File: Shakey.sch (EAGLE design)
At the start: 82 parts, among them CN1 CONN_USB-4UCON-11071, CN2 ISP, U1 ATMEGA32U4-AU, U2 ICM-20689, U3 AP2210K-3.3TRG1, Y1 16Mhz

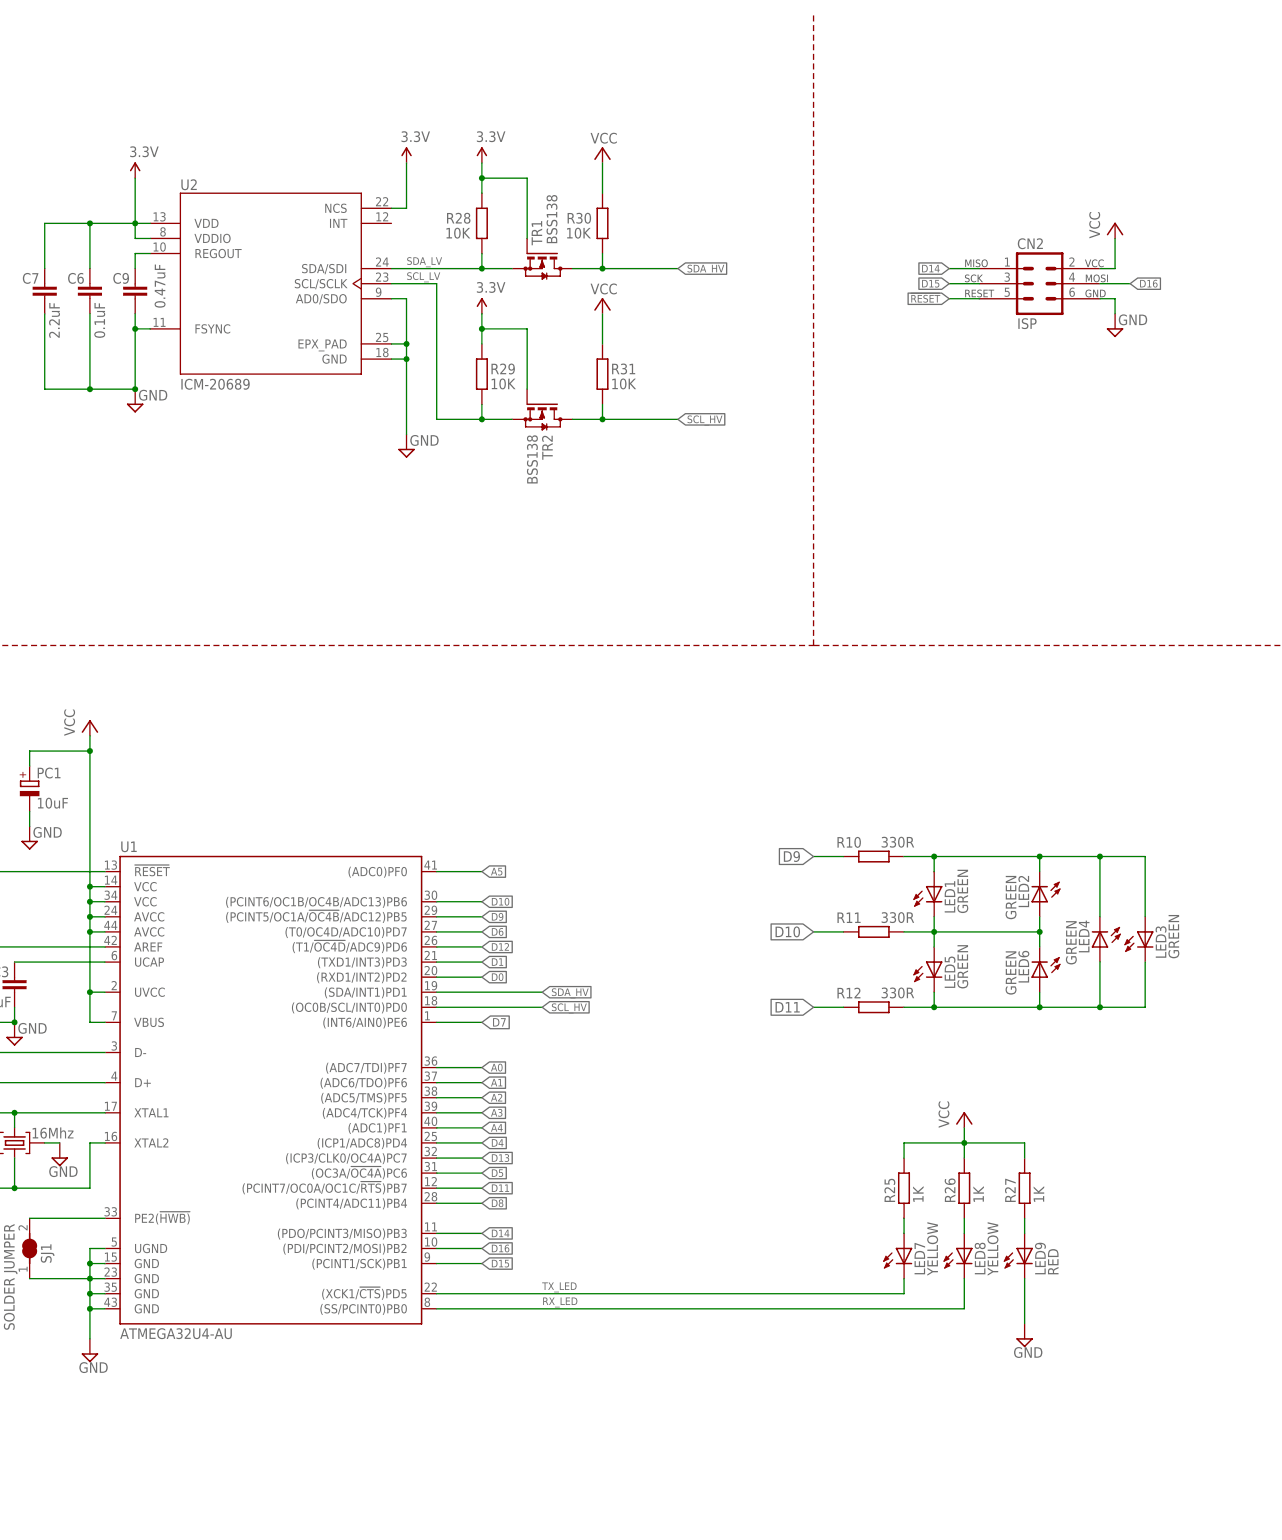
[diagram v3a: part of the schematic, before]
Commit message: added LM75
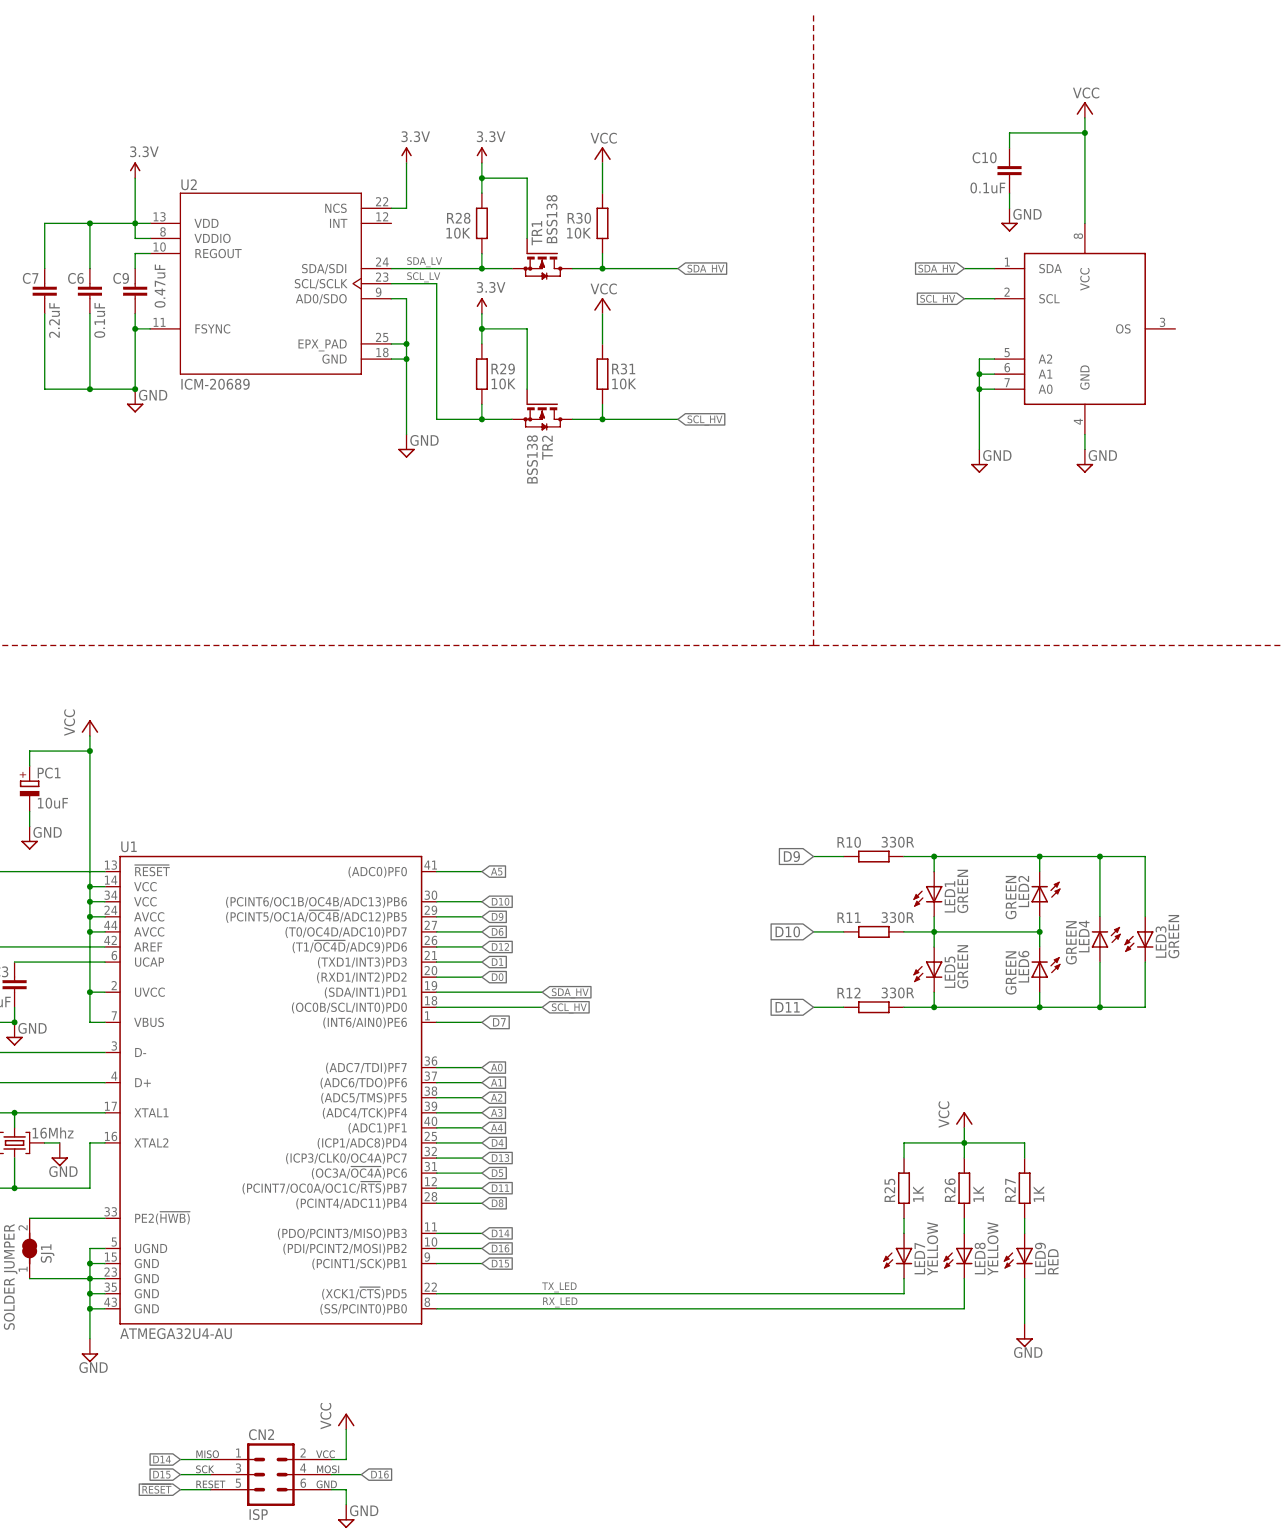
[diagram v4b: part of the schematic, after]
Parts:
- added C10: 0.1uF, rcl:C-EUC0603
- added U$6: LM75AD, SixthLogic:LM75AD
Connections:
- net GND: now also C10.1, U$6.A0, U$6.A1, U$6.A2, U$6.GND
- net SCL_HV: now also U$6.SCL
- net SDA_HV: now also U$6.SDA
- net VCC: now also C10.2, U$6.VCC
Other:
- moved on the sheet: CN2
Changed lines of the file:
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@@
 <part name="U$5" library="SixthLogic" deviceset="3.3V" device=""/>
 <part name="P+10" library="supply1" deviceset="VCC" device=""/>
+<part name="U$6" library="SixthLogic" deviceset="LM75" device="AD"/>
+<part name="SUPPLY16" library="supply2" deviceset="GND" device=""/>
+<part name="P+12" library="supply1" deviceset="VCC" device=""/>
+<part name="SUPPLY17" library="supply2" deviceset="GND" device=""/>
+<part name="C10" library="rcl" deviceset="C-EU" device="C0603" value="0.1uF"/>
+<part name="SUPPLY18" library="supply2" deviceset="GND" device=""/>
 </parts>
 <sheets>
@@
 </instance>
 <instance part="P+4" gate="VCC" x="386.08" y="149.86"/>
-<instance part="CN2" gate="G$1" x="279.4" y="228.6"/>
-<instance part="P+5" gate="VCC" x="292.1" y="238.76"/>
-<instance part="SUPPLY8" gate="GND" x="292.1" y="220.98" smashed="yes">
-<attribute name="VALUE" x="292.608" y="221.615" size="1.778" layer="96"/>
+<instance part="CN2" gate="G$1" x="149.86" y="27.94"/>
+<instance part="P+5" gate="VCC" x="162.56" y="38.1"/>
+<instance part="SUPPLY8" gate="GND" x="162.56" y="20.32" smashed="yes">
+<attribute name="VALUE" x="163.068" y="20.955" size="1.778" layer="96"/>
 </instance>
 <instance part="G" gate="G$1" x="365.76" y="167.64" smashed="yes">
@@
 <instance part="P+10" gate="VCC" x="205.74" y="226.06" smashed="yes">
 <attribute name="VALUE" x="208.28" y="228.6" size="1.778" layer="96" rot="R180"/>
+</instance>
+<instance part="U$6" gate="G$1" x="287.02" y="220.98"/>
+<instance part="SUPPLY16" gate="GND" x="287.02" y="198.12" smashed="yes">
+<attribute name="VALUE" x="287.528" y="198.755" size="1.778" layer="96"/>
+</instance>
+<instance part="P+12" gate="VCC" x="287.02" y="259.08" smashed="yes">
+<attribute name="VALUE" x="289.56" y="261.62" size="1.778" layer="96" rot="R180"/>
+</instance>
+<instance part="SUPPLY17" gate="GND" x="269.24" y="198.12" smashed="yes">
+<attribute name="VALUE" x="269.748" y="198.755" size="1.778" layer="96"/>
+</instance>
+<instance part="C10" gate="G$1" x="274.32" y="246.38" smashed="yes" rot="R180">
+<attribute name="NAME" x="267.97" y="248.92" size="1.778" layer="95"/>
+<attribute name="VALUE" x="267.589" y="243.84" size="1.778" layer="96"/>
+</instance>
+<instance part="SUPPLY18" gate="GND" x="274.32" y="238.76" smashed="yes">
+<attribute name="VALUE" x="274.828" y="239.395" size="1.778" layer="96"/>
 </instance>
 </instances>
@@
 <segment>
 <pinref part="CN2" gate="G$1" pin="6"/>
-<wire x1="289.56" y1="226.06" x2="292.1" y2="226.06" width="0.1524" layer="91"/>
-<wire x1="292.1" y1="226.06" x2="292.1" y2="223.52" width="0.1524" layer="91"/>
+<wire x1="160.02" y1="25.4" x2="162.56" y2="25.4" width="0.1524" layer="91"/>
+<wire x1="162.56" y1="25.4" x2="162.56" y2="22.86" width="0.1524" layer="91"/>
 <pinref part="SUPPLY8" gate="GND" pin="GND"/>
 </segment>
@@
 <pinref part="SUPPLY15" gate="GND" pin="GND"/>
 <wire x1="109.22" y1="139.7" x2="109.22" y2="137.16" width="0.1524" layer="91"/>
+</segment>
+<segment>
+<pinref part="U$6" gate="G$1" pin="GND"/>
+<pinref part="SUPPLY16" gate="GND" pin="GND"/>
+<wire x1="287.02" y1="203.2" x2="287.02" y2="200.66" width="0.1524" layer="91"/>
+</segment>
+<segment>
+<pinref part="U$6" gate="G$1" pin="A2"/>
+<wire x1="271.78" y1="215.9" x2="269.24" y2="215.9" width="0.1524" layer="91"/>
+<wire x1="269.24" y1="215.9" x2="269.24" y2="213.36" width="0.1524" layer="91"/>
+<pinref part="U$6" gate="G$1" pin="A1"/>
+<wire x1="269.24" y1="213.36" x2="269.24" y2="210.82" width="0.1524" layer="91"/>
+<wire x1="269.24" y1="210.82" x2="269.24" y2="200.66" width="0.1524" layer="91"/>
+<wire x1="271.78" y1="213.36" x2="269.24" y2="213.36" width="0.1524" layer="91"/>
+<junction x="269.24" y="213.36"/>
+<pinref part="U$6" gate="G$1" pin="A0"/>
+<wire x1="271.78" y1="210.82" x2="269.24" y2="210.82" width="0.1524" layer="91"/>
+<junction x="269.24" y="210.82"/>
+<pinref part="SUPPLY17" gate="GND" pin="GND"/>
+</segment>
+<segment>
+<pinref part="SUPPLY18" gate="GND" pin="GND"/>
+<pinref part="C10" gate="G$1" pin="1"/>
+<wire x1="274.32" y1="241.3" x2="274.32" y2="243.84" width="0.1524" layer="91"/>
 </segment>
 </net>
@@
 <segment>
 <pinref part="CN2" gate="G$1" pin="2"/>
-<wire x1="289.56" y1="231.14" x2="292.1" y2="231.14" width="0.1524" layer="91"/>
+<wire x1="160.02" y1="30.48" x2="162.56" y2="30.48" width="0.1524" layer="91"/>
 <pinref part="P+5" gate="VCC" pin="VCC"/>
-<wire x1="292.1" y1="236.22" x2="292.1" y2="231.14" width="0.1524" layer="91"/>
+<wire x1="162.56" y1="35.56" x2="162.56" y2="30.48" width="0.1524" layer="91"/>
 </segment>
 <segment>
@@
 <wire x1="205.74" y1="223.52" x2="205.74" y2="218.44" width="0.1524" layer="91"/>
 </segment>
+<segment>
+<pinref part="P+12" gate="VCC" pin="VCC"/>
+<pinref part="U$6" gate="G$1" pin="VCC"/>
+<wire x1="287.02" y1="256.54" x2="287.02" y2="254" width="0.1524" layer="91"/>
+<pinref part="C10" gate="G$1" pin="2"/>
+<wire x1="287.02" y1="254" x2="287.02" y2="238.76" width="0.1524" layer="91"/>
+<wire x1="274.32" y1="251.46" x2="274.32" y2="254" width="0.1524" layer="91"/>
+<wire x1="274.32" y1="254" x2="287.02" y2="254" width="0.1524" layer="91"/>
+<junction x="287.02" y="254"/>
+</segment>
 </net>
 <net name="N$5" class="0">
@@
 <segment>
 <pinref part="CN2" gate="G$1" pin="5"/>
-<wire x1="269.24" y1="226.06" x2="264.16" y2="226.06" width="0.1524" layer="91"/>
-<label x="264.16" y="226.06" size="1.27" layer="95" rot="R180" xref="yes"/>
+<wire x1="139.7" y1="25.4" x2="134.62" y2="25.4" width="0.1524" layer="91"/>
+<label x="134.62" y="25.4" size="1.27" layer="95" rot="R180" xref="yes"/>
 </segment>
 </net>
@@
 <segment>
 <pinref part="CN2" gate="G$1" pin="3"/>
-<wire x1="269.24" y1="228.6" x2="264.16" y2="228.6" width="0.1524" layer="91"/>
-<label x="264.16" y="228.6" size="1.27" layer="95" rot="R180" xref="yes"/>
+<wire x1="139.7" y1="27.94" x2="134.62" y2="27.94" width="0.1524" layer="91"/>
+<label x="134.62" y="27.94" size="1.27" layer="95" rot="R180" xref="yes"/>
 </segment>
 </net>
@@
 <segment>
 <pinref part="CN2" gate="G$1" pin="1"/>
-<wire x1="269.24" y1="231.14" x2="264.16" y2="231.14" width="0.1524" layer="91"/>
-<label x="264.16" y="231.14" size="1.27" layer="95" rot="R180" xref="yes"/>
+<wire x1="139.7" y1="30.48" x2="134.62" y2="30.48" width="0.1524" layer="91"/>
+<label x="134.62" y="30.48" size="1.27" layer="95" rot="R180" xref="yes"/>
 </segment>
 </net>
@@
 <segment>
 <pinref part="CN2" gate="G$1" pin="4"/>
-<wire x1="289.56" y1="228.6" x2="294.64" y2="228.6" width="0.1524" layer="91"/>
-<label x="294.64" y="228.6" size="1.27" layer="95" xref="yes"/>
+<wire x1="160.02" y1="27.94" x2="165.1" y2="27.94" width="0.1524" layer="91"/>
+<label x="165.1" y="27.94" size="1.27" layer="95" xref="yes"/>
 </segment>
 </net>
@@
 <label x="195.58" y="109.22" size="1.27" layer="95" xref="yes"/>
 </segment>
+<segment>
+<pinref part="U$6" gate="G$1" pin="SDA"/>
+<wire x1="271.78" y1="231.14" x2="266.7" y2="231.14" width="0.1524" layer="91"/>
+<label x="266.7" y="231.14" size="1.27" layer="95" rot="R180" xref="yes"/>
+</segment>
 </net>
 <net name="SCL_HV" class="0">
@@
 <label x="195.58" y="106.68" size="1.27" layer="95" xref="yes"/>
 </segment>
-</net>
+<segment>
+<pinref part="U$6" gate="G$1" pin="SCL"/>
+<wire x1="271.78" y1="226.06" x2="266.7" y2="226.06" width="0.1524" layer="91"/>
+<label x="266.7" y="226.06" size="1.27" layer="95" rot="R180" xref="yes"/>
+</segment>
+</net>

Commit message: 90 percent parts placed
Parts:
- removed EARTH6: MA01-1-ALLIGATOR-3MM, SixthLogic:MA01-1-ALLIGATOR-3MM
- removed R15, R16: 22M, rcl:R-EU_R0603
- LED7, LED8, LED9: device led:LEDCHIPLED_0603 -> SixthLogic:LED-1206-LTST-BOTTOM
- renumbered LED1 to LED_DOWN, LED2 to LED_LEFT, LED3 to LED_CLICK, LED4 to LED_SPACE, LED5 to LED_UP, LED6 to LED_RIGHT, U$6 to U4
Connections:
- net 3.3V: now also C10.2, U4.VCC
- net GND: no longer EARTH6.1
- net SCL_HV: no longer U4.SCL
- net SCL_LV: now also U4.SCL
- net SDA_HV: no longer U4.SDA
- net SDA_LV: now also U4.SDA
- net VCC: no longer C10.2, R15.2, R16.2, U4.VCC
